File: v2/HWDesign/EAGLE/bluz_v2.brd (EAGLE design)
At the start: 20.3 x 35.6 mm, 26 parts, among them Q1 FC-12M, U1 MDBT40SMD, U3 MCP1700T-3302E/TT

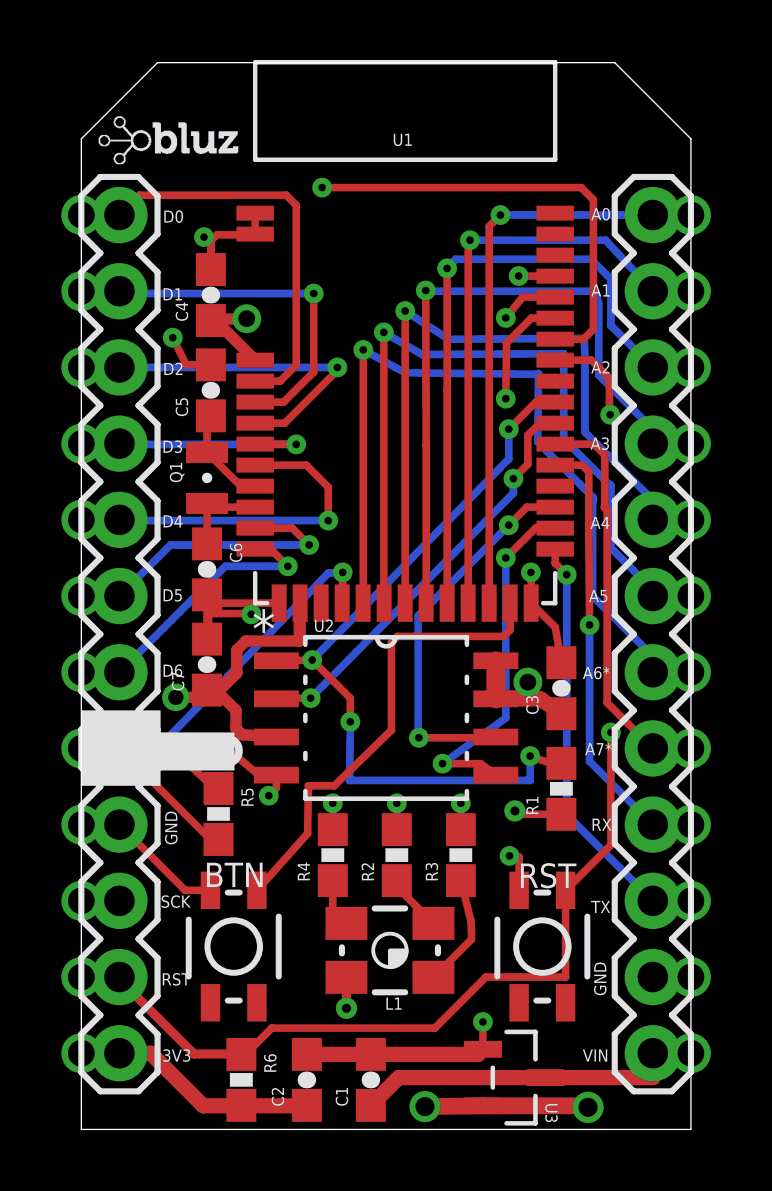
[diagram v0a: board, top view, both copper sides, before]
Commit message: cleaned up some issues. filled remaining top layer with ground
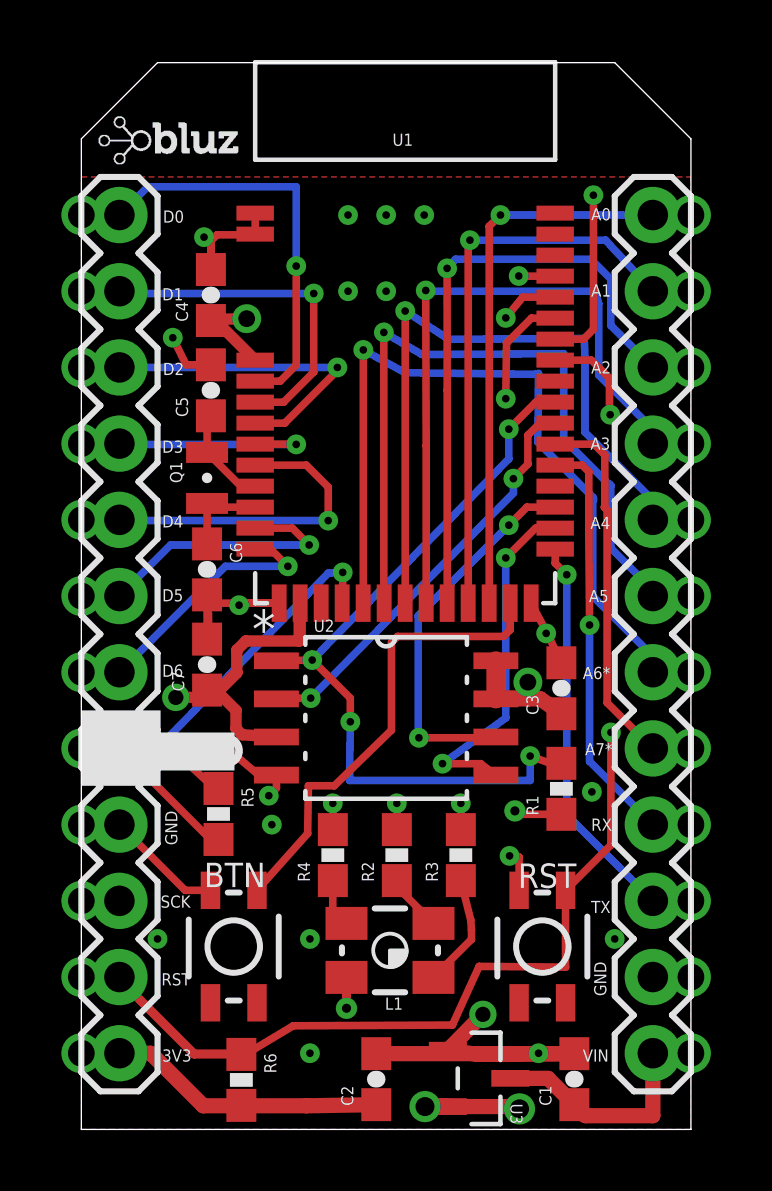
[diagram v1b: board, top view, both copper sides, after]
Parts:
- moved C1 6.78 mm to (16.4, 1.68)
- moved C2 2.31 mm to (9.83, 1.68)
- moved U3 1.17 mm to (13.3, 1.70)
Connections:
- net GND: now also U1.42
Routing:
- net GND: track 37.0 -> 44.2 mm, vias 7 -> 18
- net RAW: track 10.6 -> 7.35 mm
- net VCC: track 47.3 -> 48.6 mm
- net D0: track 13.2 -> 13.8 mm, vias 0 -> 1
- added copper zone on layer 1, net GND

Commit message: change part number for LDO in BOM. update PCB. script for generating gerbers
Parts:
- moved C2 0.56 mm to (9.27, 1.68)
- moved U3 0.05 mm to (13.2, 1.70)
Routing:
- net GND: track 44.2 -> 52.8 mm
- net VCC: track 48.6 -> 49.8 mm
- net BTN: track 15.6 -> 16.3 mm, vias 0 -> 2
- net RST: track 39.8 -> 40.4 mm
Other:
- board text added: "Bluz DK v2 rev A"

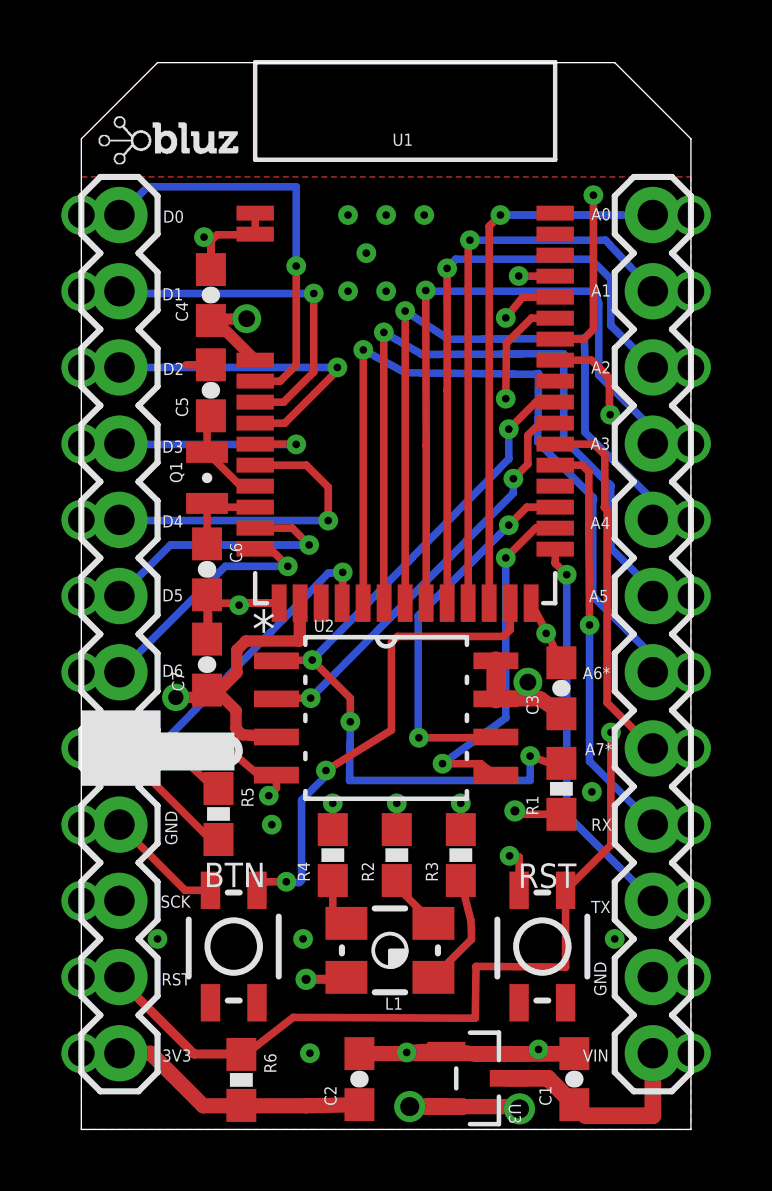
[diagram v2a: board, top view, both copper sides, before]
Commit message: fix an issue on the PCB
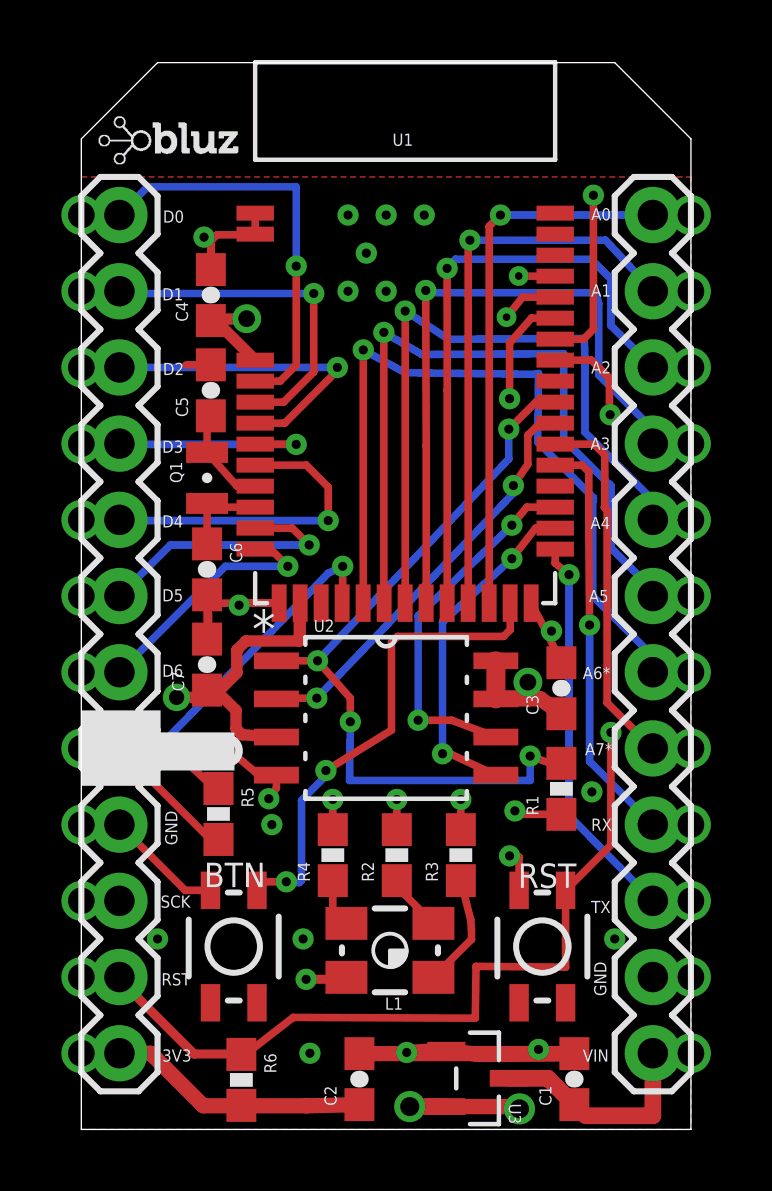
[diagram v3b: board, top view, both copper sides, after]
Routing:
- net GND: track 52.8 -> 45.3 mm, vias 18 -> 19

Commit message: larger silkscreen. remove labels. copper on bottom of castellated edges. move buttons further in
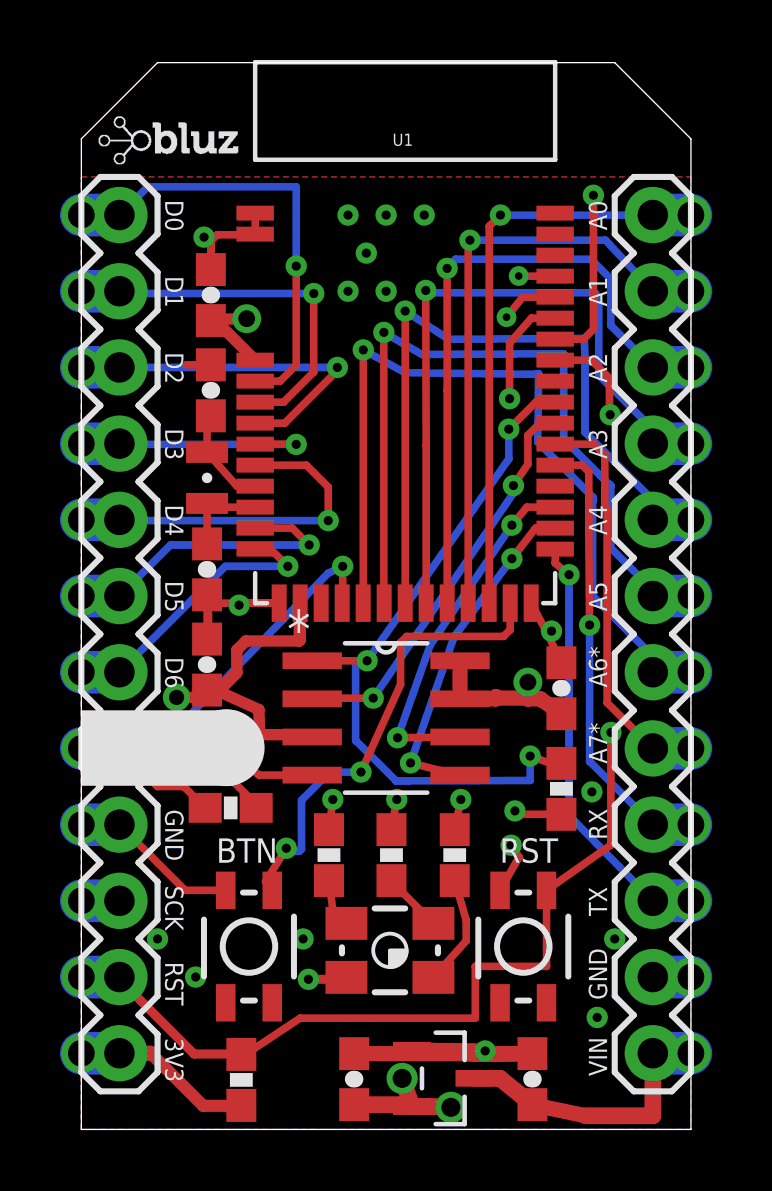
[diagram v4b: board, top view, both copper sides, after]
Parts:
- removed U2: (no value), Silicon_Storage_Tech_By_element14_Batch_1:SOIC127P790X216-8N
- added U4: SST25VF010A-33-4I-SAE, Silicon_Storage_Tech_By_element14_Batch_1:SOIC127P600X175-8N
- R1: value (none) -> 1k
- R6: value (none) -> 10k
- moved C1 1.40 mm to (15.0, 1.68)
- moved U3 1.14 mm to (12.1, 1.70)
- moved RST 0.64 mm to (14.7, 6.10)
- moved LED2 0.53 mm to (4.34, 12.6)
- moved BTN 0.51 mm to (5.59, 6.10)
- moved R5 0.45 mm to (4.98, 10.7), turned to 180 degrees
- moved R3 0.20 mm to (12.4, 9.14)
- moved C2 0.18 mm to (9.09, 1.68)
- moved R2 0.18 mm to (10.3, 9.14)
- moved R4 0.13 mm to (8.26, 9.14)
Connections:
- net GND: now also U4.4; no longer U2.4
- net SPI_MISO: now also U4.2; no longer U2.2
- net SPI_MOSI: now also U4.5; no longer U2.5
- net SPI_SCK: now also U4.6; no longer U2.6
- net SPI_SS: now also U4.1; no longer U2.1
- net VCC: now also U4.3, U4.7, U4.8; no longer U2.3, U2.7, U2.8
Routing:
- net RAW: track 7.40 -> 9.65 mm, vias 0 -> 1
- net LED2: track 22.6 -> 24.5 mm
- net SPI_SS: track 25.9 -> 24.3 mm, vias 4 -> 3
- net SWCLK: track 44.1 -> 45.4 mm, vias 1 -> 2
- net TX: track 13.1 -> 14.4 mm, vias 1 -> 2
- net RX: track 13.8 -> 15.1 mm, vias 1 -> 2
- net D6: track 8.40 -> 9.67 mm, vias 1 -> 2
- net D5: track 9.06 -> 10.3 mm, vias 1 -> 2
- net D4: track 10.8 -> 12.1 mm, vias 1 -> 2
- net D3: track 7.27 -> 8.54 mm, vias 1 -> 2
- net D2: track 10.8 -> 12.1 mm, vias 1 -> 2
- net D1: track 11.5 -> 12.8 mm, vias 1 -> 2
- net D0: track 13.8 -> 15.1 mm, vias 1 -> 2
- net A7: track 12.3 -> 13.5 mm, vias 0 -> 1
- net A6: track 26.1 -> 27.4 mm, vias 1 -> 2
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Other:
- board text added: "Bluz DK v2 rev C"
- board text added: "D7"
- board text removed: "Bluz DK v2 rev A"

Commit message: updated RGB LED to new part. changed resistors for new LED. updated labeling on bluz.
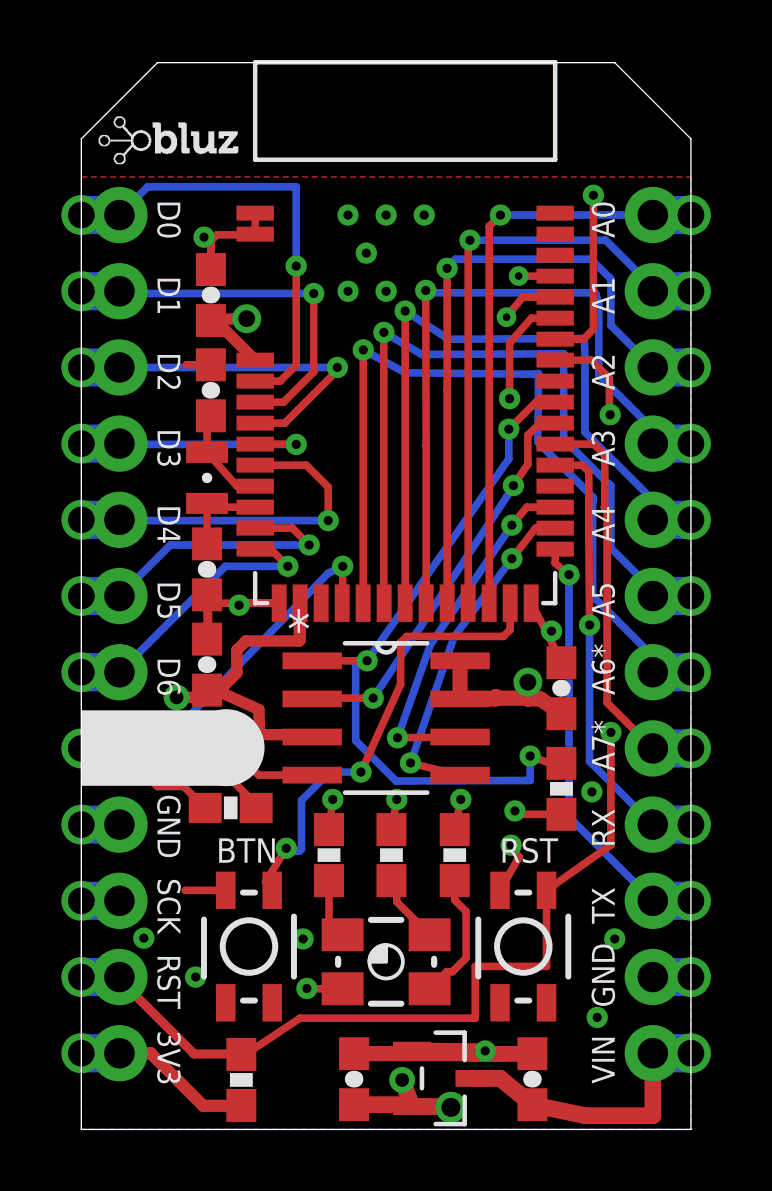
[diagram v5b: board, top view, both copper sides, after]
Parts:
- removed L1: (no value), Spark:P-LCC-4-3
- added LED1: (no value), bluze_libr:P-LCC-4-3
- JP1, JP2: value M12PTH -> M121X12_NO_SILK_KIT; device SparkFun-Connectors:1X12 -> SparkFun-Connectors:1X12_NO_SILK_KIT
- R1: value 1k -> 4.7K; device SparkFun-Resistors:0603-RES -> SparkFun-Passives:0603-RES
- R2, R3: value 1K -> 4.7K
- R4: value 1K -> 1k; device SparkFun-Passives:0603-RES -> SparkFun-Resistors:0603-RES
- moved R4 8.06 mm to (16.0, 11.4)
- moved R1 6.08 mm to (10.3, 9.14)
- moved R3 4.19 mm to (8.26, 9.14)
- moved R2 2.11 mm to (12.4, 9.14)
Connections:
- net LED2: now also R3.2; no longer R4.2
- net LED3: now also R1.2; no longer R2.2
- net LED4: now also R2.2; no longer R3.2
- net N$5: now also LED1.1, R3.1; no longer L1.1, R4.1
- net N$6: now also LED1.3, R2.1; no longer L1.3, R3.1
- net N$7: now also LED1.4, R1.1; no longer L1.4, R2.1
- net SPI_SS: now also R4.2; no longer R1.2
- net VCC: now also LED1.2, R4.1; no longer L1.2, R1.1
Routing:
- net GND: track 46.1 -> 43.0 mm
- net VCC: track 49.0 -> 48.2 mm
- net N$6: track 3.70 -> 4.38 mm

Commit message: cleanup some naming mistakes. properly labeled all capacitors
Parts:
- removed BTN, RST: (no value), Spark:TACTILE_SWITCH_SMD
- added S1, S2: (no value), Spark:TACTILE_SWITCH_SMD
- C3: value .1uF -> 1uF
- C4: value 1uF -> .1uF
- C5: value 12pF -> .1uF
- C7: value .1uF -> 12pF
- moved C3 17.6 mm to (4.32, 27.8)
- moved C4 17.6 mm to (16.0, 14.7)
- moved C5 9.14 mm to (4.19, 15.5)
- moved C7 9.14 mm to (4.32, 24.6)
- renumbered LED1 to L1, LED2 to L2, U4 to U2
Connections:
- net BTN: now also S1.4; no longer BTN.4
- net GND: now also S1.2, S2.2; no longer BTN.2, RST.2
- net N$2: now also C7.1; no longer C5.1
- net RST: now also S2.4; no longer RST.4
- net VCC: now also C5.1; no longer C7.1
